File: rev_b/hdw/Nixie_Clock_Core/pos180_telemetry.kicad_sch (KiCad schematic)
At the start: 25 parts

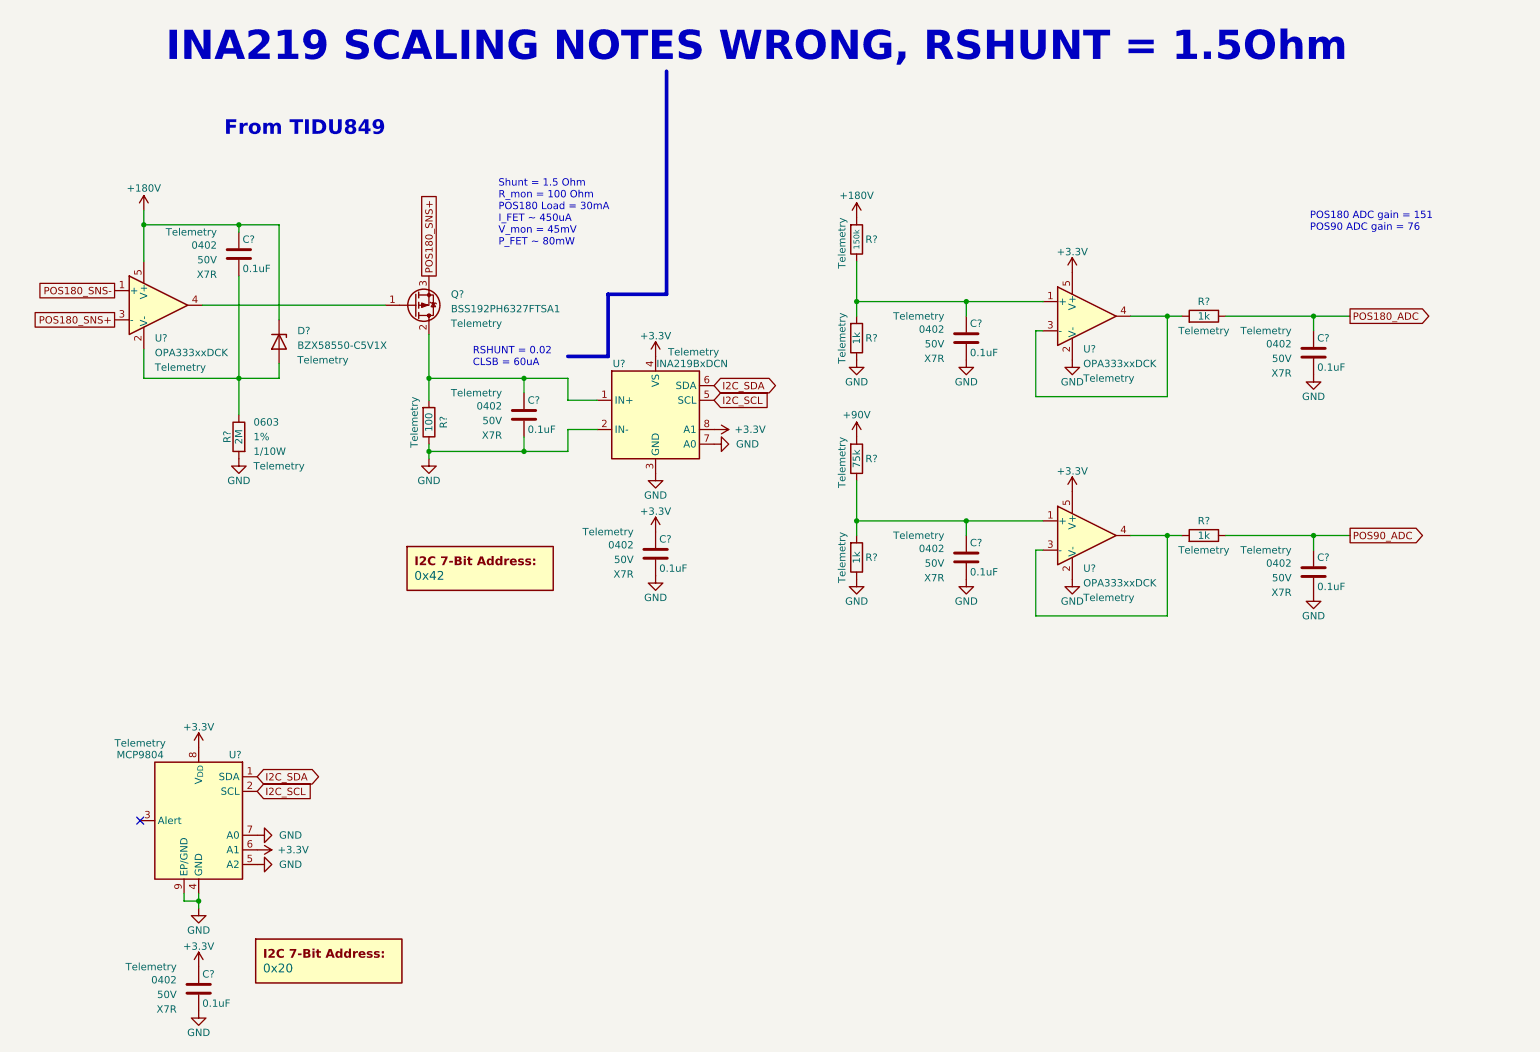
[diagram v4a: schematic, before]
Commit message: updated footprints, ran some DRC
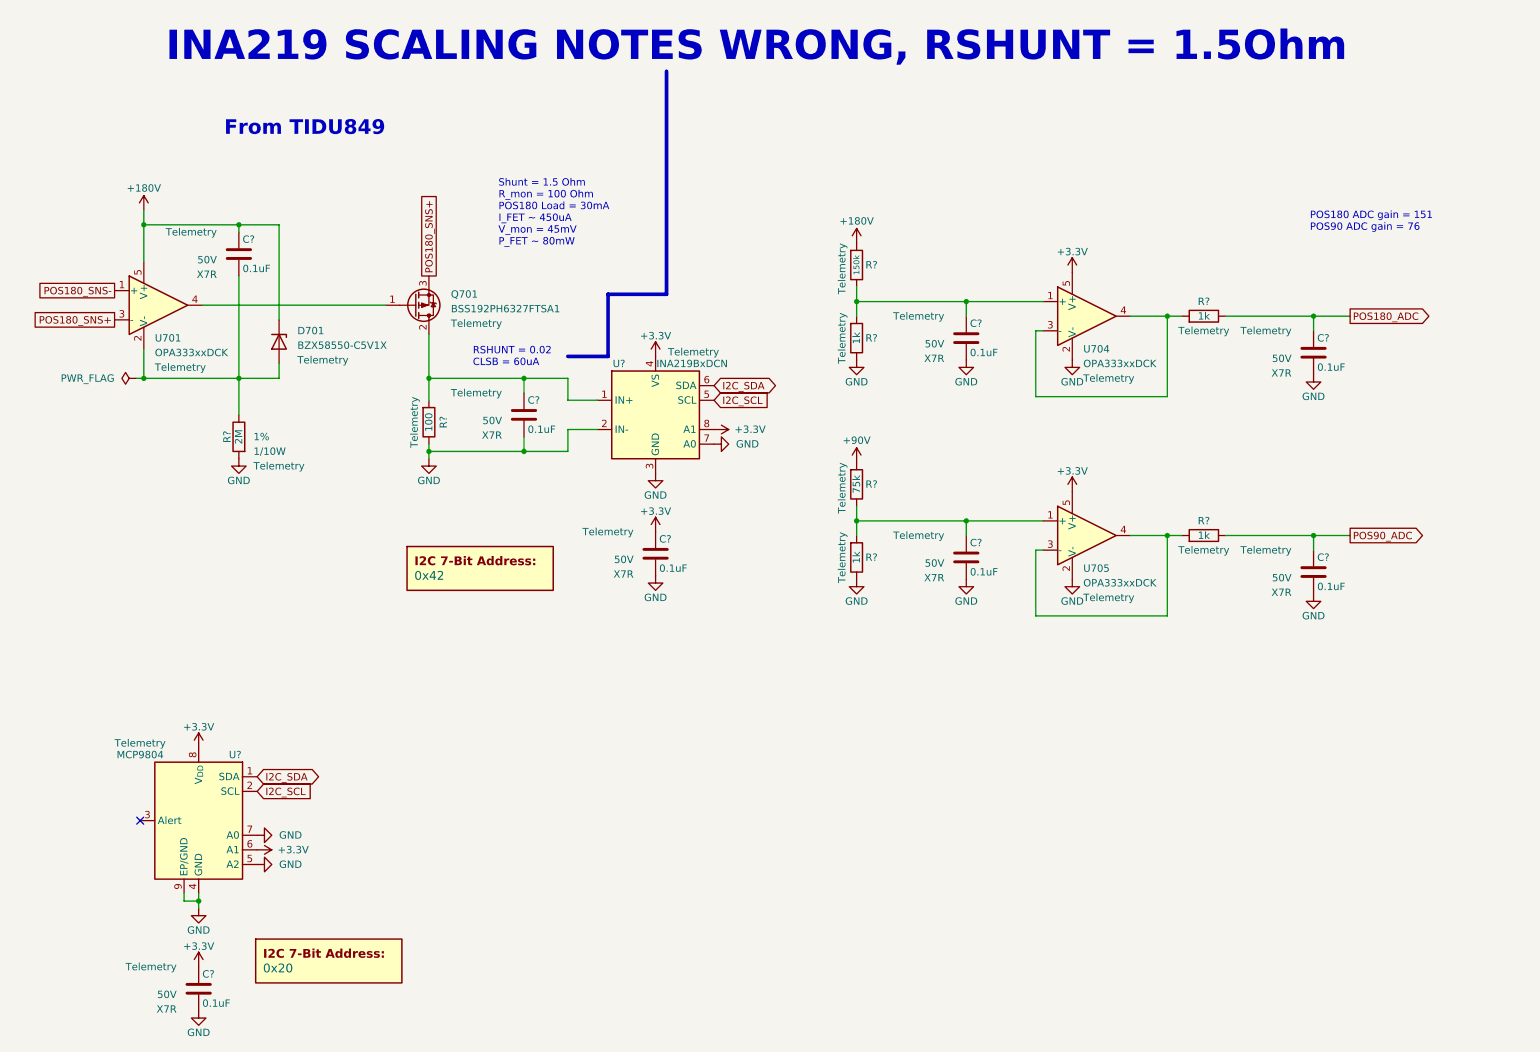
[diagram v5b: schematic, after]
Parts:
- C? (x8): footprint Capacitors_SMD:C_0402 -> Capacitors_SMD:C_0603; Digi-Key PN 490-10698-1-ND -> (none); display_footprint 0402 -> (none)
- R? (x3): footprint Resistors_SMD:R_0402 -> Resistors_SMD:R_0603; Wattage 1/16W -> 1/10W; display_footprint 0402 -> 0603
- R? (x4): footprint Resistors_SMD:R_0402 -> Resistors_SMD:R_0603; Digi-Key PN RMCF0402FT1K00CT-ND -> (none); Wattage 1/16W -> 1/10W; display_footprint 0402 -> 0603
- R?: Footprint Display 0603 -> (none); display_footprint (none) -> 0603
- gave numbers to parts that had none: 5
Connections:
- net POS180_ADC: now also C?.1, R?.2
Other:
- moved on the sheet: R?

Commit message: hid all passive refdes on core PCB
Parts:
- C? (x8): Digi-Key PN (none) -> 1276-1935-1-ND; display_footprint (none) -> 0603
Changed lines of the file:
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@@
       (effects (font (size 1.27 1.27)) hide)
     )
-    (property "display_footprint" "" (at 121.92 115.951 0)
+    (property "display_footprint" "0603" (at 121.92 115.951 0)
       (effects (font (size 1.27 1.27)) (justify right))
     )
@@
       (effects (font (size 1.27 1.27)) (justify right))
     )
-    (property "Digi-Key PN" "" (at 125.73 117.475 0)
+    (property "Digi-Key PN" "1276-1935-1-ND" (at 125.73 117.475 0)
       (effects (font (size 1.27 1.27)) hide)
     )
@@
       (effects (font (size 1.27 1.27)) hide)
     )
-    (property "display_footprint" "" (at 42.545 191.516 0)
+    (property "display_footprint" "0603" (at 42.545 191.516 0)
       (effects (font (size 1.27 1.27)) (justify right))
     )
@@
       (effects (font (size 1.27 1.27)) (justify right))
     )
-    (property "Digi-Key PN" "" (at 46.355 193.04 0)
+    (property "Digi-Key PN" "1276-1935-1-ND" (at 46.355 193.04 0)
       (effects (font (size 1.27 1.27)) hide)
     )
@@
       (effects (font (size 1.27 1.27)) hide)
     )
-    (property "display_footprint" "" (at 236.22 119.126 0)
+    (property "display_footprint" "0603" (at 236.22 119.126 0)
       (effects (font (size 1.27 1.27)) (justify right))
     )
@@
       (effects (font (size 1.27 1.27)) (justify right))
     )
-    (property "Digi-Key PN" "" (at 240.03 120.65 0)
+    (property "Digi-Key PN" "1276-1935-1-ND" (at 240.03 120.65 0)
       (effects (font (size 1.27 1.27)) hide)
     )
@@
       (effects (font (size 1.27 1.27)) hide)
     )
-    (property "display_footprint" "" (at 99.06 91.821 0)
+    (property "display_footprint" "0603" (at 99.06 91.821 0)
       (effects (font (size 1.27 1.27)) (justify right))
     )
@@
       (effects (font (size 1.27 1.27)) (justify right))
     )
-    (property "Digi-Key PN" "" (at 102.87 93.345 0)
+    (property "Digi-Key PN" "1276-1935-1-ND" (at 102.87 93.345 0)
       (effects (font (size 1.27 1.27)) hide)
     )
@@
       (effects (font (size 1.27 1.27)) hide)
     )
-    (property "display_footprint" "" (at 236.22 81.026 0)
+    (property "display_footprint" "0603" (at 236.22 81.026 0)
       (effects (font (size 1.27 1.27)) (justify right))
     )
@@
       (effects (font (size 1.27 1.27)) (justify right))
     )
-    (property "Digi-Key PN" "" (at 240.03 82.55 0)
+    (property "Digi-Key PN" "1276-1935-1-ND" (at 240.03 82.55 0)
       (effects (font (size 1.27 1.27)) hide)
     )
@@
       (effects (font (size 1.27 1.27)) hide)
     )
-    (property "display_footprint" "" (at 175.895 78.486 0)
+    (property "display_footprint" "0603" (at 175.895 78.486 0)
       (effects (font (size 1.27 1.27)) (justify right))
     )
@@
       (effects (font (size 1.27 1.27)) (justify right))
     )
-    (property "Digi-Key PN" "" (at 179.705 80.01 0)
+    (property "Digi-Key PN" "1276-1935-1-ND" (at 179.705 80.01 0)
       (effects (font (size 1.27 1.27)) hide)
     )
@@
       (effects (font (size 1.27 1.27)) hide)
     )
-    (property "display_footprint" "" (at 49.53 63.881 0)
+    (property "display_footprint" "0603" (at 49.53 63.881 0)
       (effects (font (size 1.27 1.27)) (justify right))
     )
@@
       (effects (font (size 1.27 1.27)) (justify right))
     )
-    (property "Digi-Key PN" "" (at 53.34 65.405 0)
+    (property "Digi-Key PN" "1276-1935-1-ND" (at 53.34 65.405 0)
       (effects (font (size 1.27 1.27)) hide)
     )
@@
       (effects (font (size 1.27 1.27)) hide)
     )
-    (property "display_footprint" "" (at 175.895 116.586 0)
+    (property "display_footprint" "0603" (at 175.895 116.586 0)
       (effects (font (size 1.27 1.27)) (justify right))
     )
@@
       (effects (font (size 1.27 1.27)) (justify right))
     )
-    (property "Digi-Key PN" "" (at 179.705 118.11 0)
-      (effects (font (size 1.27 1.27)) hide)
-    )
+    (property "Digi-Key PN" "1276-1935-1-ND" (at 179.705 118.11 0)
+      (effects (font (size 1.27 1.27)) hide)
+    )

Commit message: lots more PCB placement
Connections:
- net +180V: no longer R?.1
- new net +90V: R?.1
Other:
- moved on the sheet: C?, D701, Q701, R?, U701, U?

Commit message: lots of core board routing
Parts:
- added C? (x2): 0.1uF, Capacitors_SMD:C_0603, symbol Custom_Library:C_Custom
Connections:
- net +3.3V: now also C?.1, C?.1
- net GND: now also C?.2, C?.2
